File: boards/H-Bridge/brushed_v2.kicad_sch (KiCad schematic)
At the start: 14 parts, among them IC1 TC1108-3.3VDBTR, J1 Prog_Header, J2 CANBus, J3 UART, J4 Encoder, U1 STM32F103C8Tx

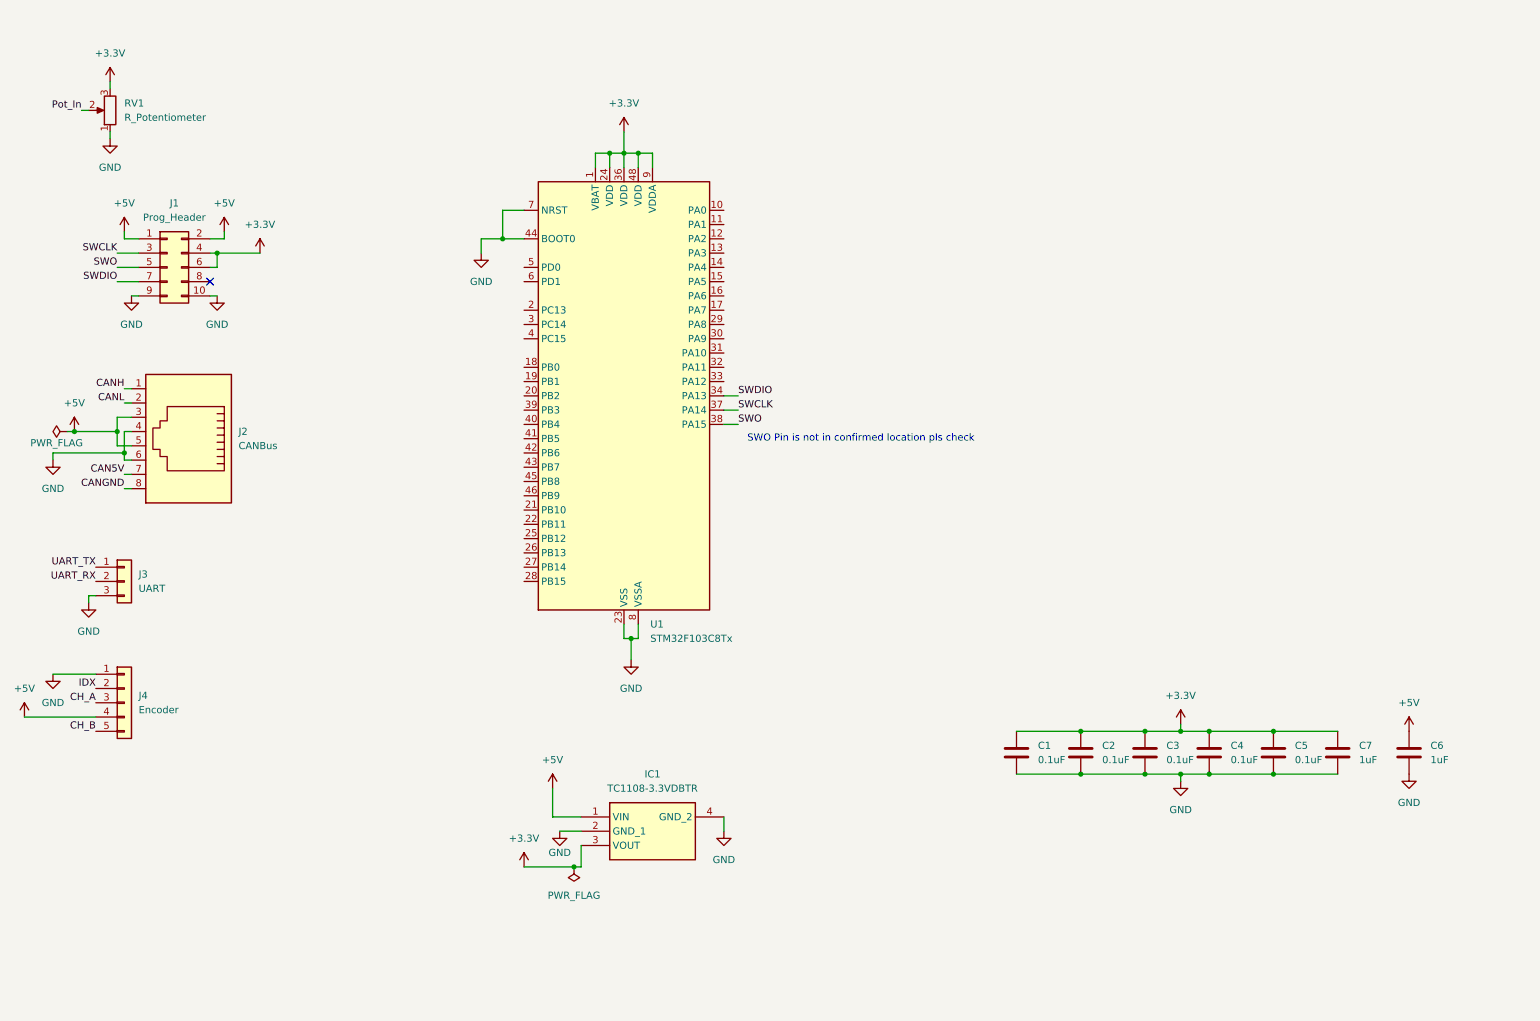
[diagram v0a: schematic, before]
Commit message: Add new sheet for HV, add components
also figured out hierarchical labels
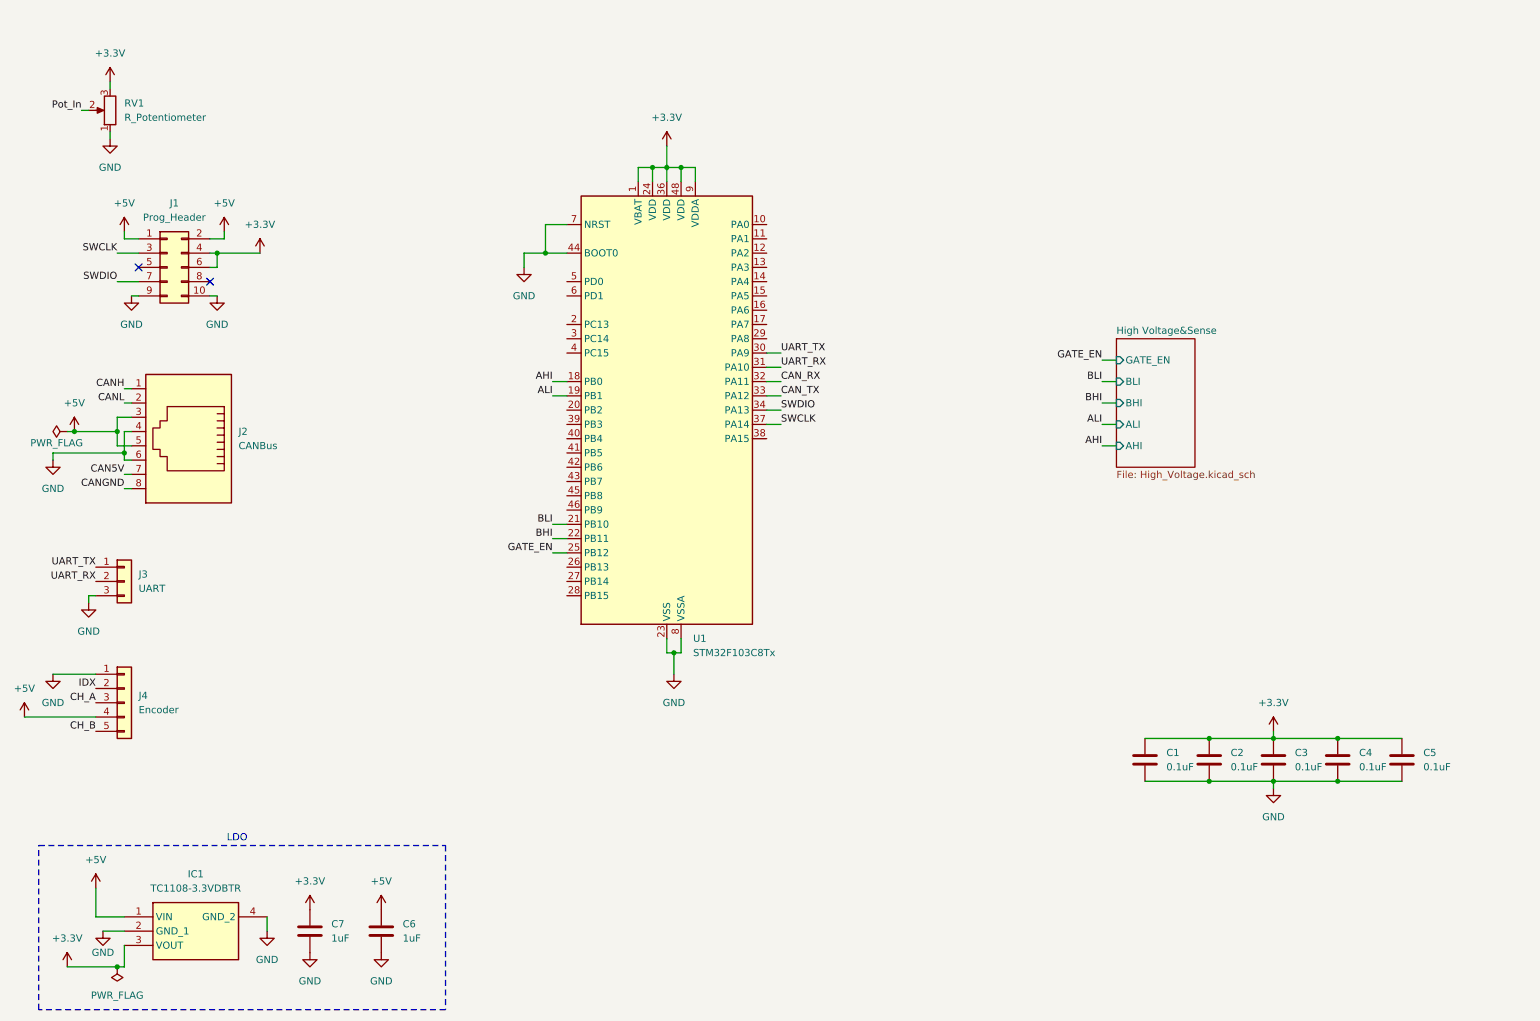
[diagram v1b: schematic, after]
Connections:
- net UART_RX: now also U1.31 (PA10)
- net UART_TX: now also U1.30 (PA9)
- net AHI: now reaches U1.18 (PB0)
- net ALI: now reaches U1.19 (PB1)
- net BLI: now reaches U1.21 (PB10)
- net BHI: now reaches U1.22 (PB11)
- net GATE_EN: now reaches U1.25 (PB12)
- net CAN_RX: now reaches U1.32 (PA11)
- net CAN_TX: now reaches U1.33 (PA12)
- net SWO: no longer names the net of J1.5 (Pin_5)
- net SWO: no longer U1.38 (PA15)
- no-connect marks 1 -> 2
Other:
- added sheet High Voltage&Sense (High_Voltage.kicad_sch)
- note added: "LDO"
- note removed: "SWO Pin is not in confirmed location pls check"
- moved on the sheet: C1, C2, C3, C4, C5, C6, IC1, U1

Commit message: Added symbols + fixed sheet layout, low voltage nearly complete
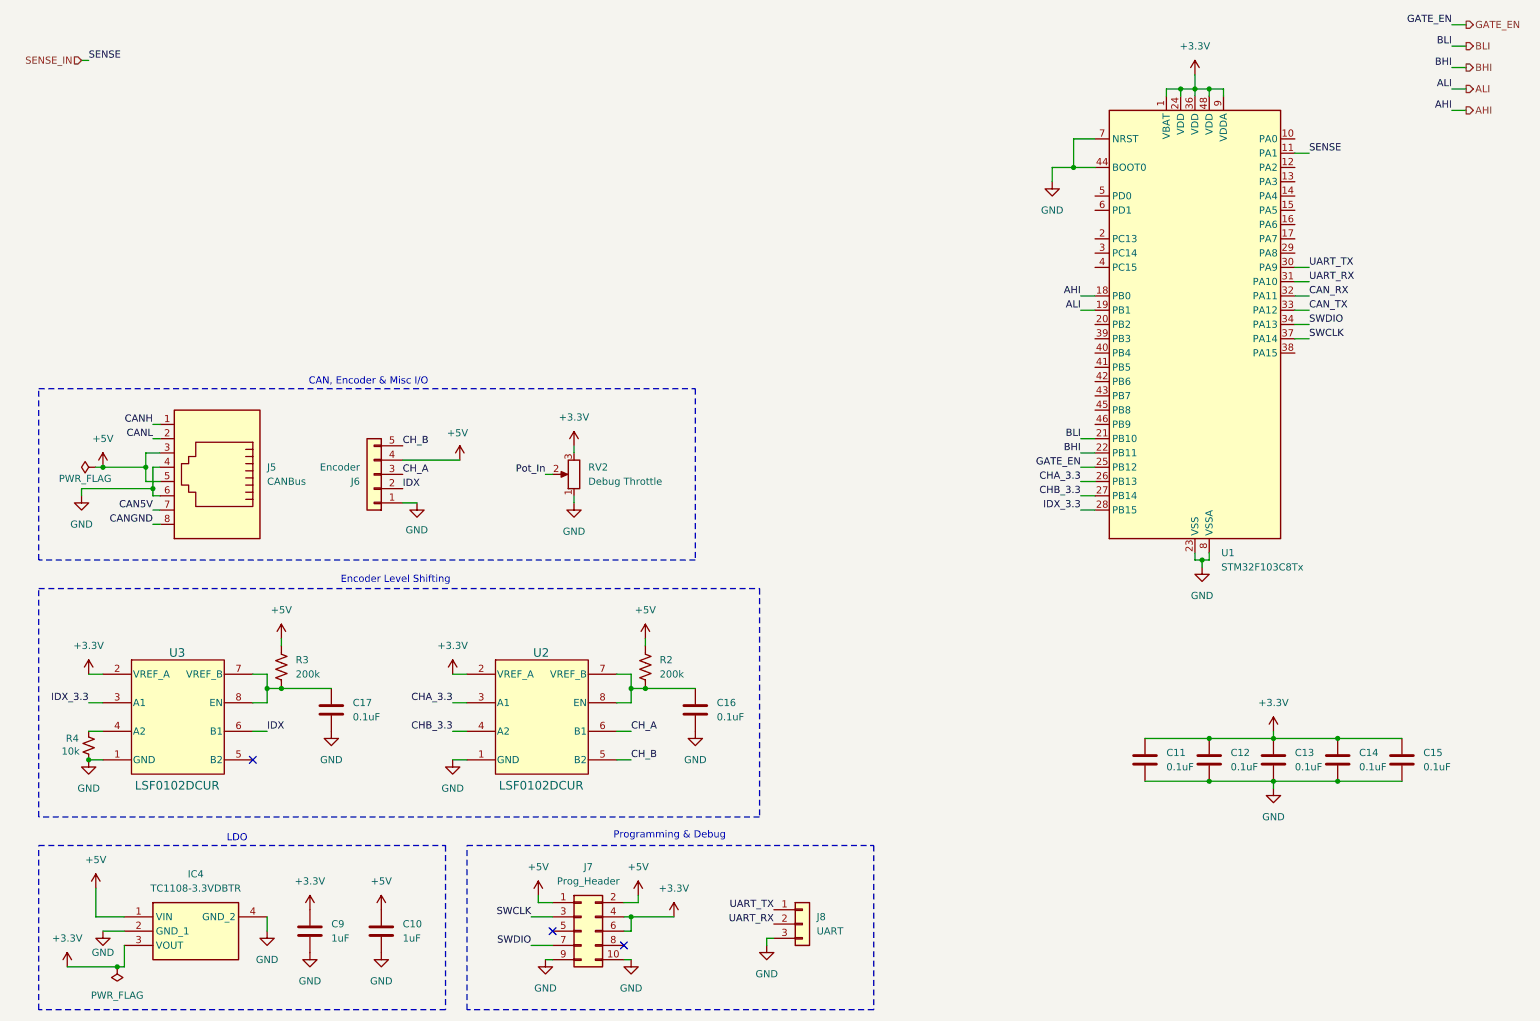
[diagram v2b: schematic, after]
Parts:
- added C16, C17: 0.1uF, symbol Device:C
- added R2, R3: 200k, symbol Device:R_US
- added R4: 10k, symbol Device:R_Small_US
- added U2, U3: LSF0102DCUR, DCU0008A_N, symbol Level_Shifters:LSF0102DCUR
- RV2: renamed from RV1; value R_Potentiometer -> Debug Throttle
- renumbered C6 to C10, C1 to C11, C2 to C12, C3 to C13, C4 to C14, C5 to C15, C7 to C9, IC1 to IC4, J2 to J5, J4 to J6, J1 to J7, J3 to J8
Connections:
- net +3.3V: now also U2.2 (VREF_A), U3.2 (VREF_A)
- net +5V: now also R2.1, R3.1
- net CH_A: now also U2.6 (B1)
- net CH_B: now also U2.5 (B2)
- net GND: now also C16.2, C17.2, R4.1, U2.1 (GND), U3.1 (GND)
- net IDX: now also U3.6 (B1)
- net SENSE_IN: now reaches U1.11 (PA1)
- net CHA_3.3: now reaches U1.26 (PB13)
- net CHA_3.3: now also U2.3 (A1)
- net CHB_3.3: now reaches U1.27 (PB14)
- net CHB_3.3: now also U2.4 (A2)
- net IDX_3.3: now reaches U1.28 (PB15)
- net IDX_3.3: now also U3.3 (A1)
- new net: C17.1, R3.2, U3.7 (VREF_B), U3.8 (EN)
- new net: R4.2, U3.4 (A2)
- new net: C16.1, R2.2, U2.7 (VREF_B), U2.8 (EN)
- no-connect marks 2 -> 3
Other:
- removed sheet High Voltage&Sense
- note added: "CAN, Encoder & Misc I/O"
- note added: "Encoder Level Shifting"
- note added: "Programming & Debug"
- moved on the sheet: J5, J6, J7, J8, RV2, U1

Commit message: finished schematic (i think), added footprints
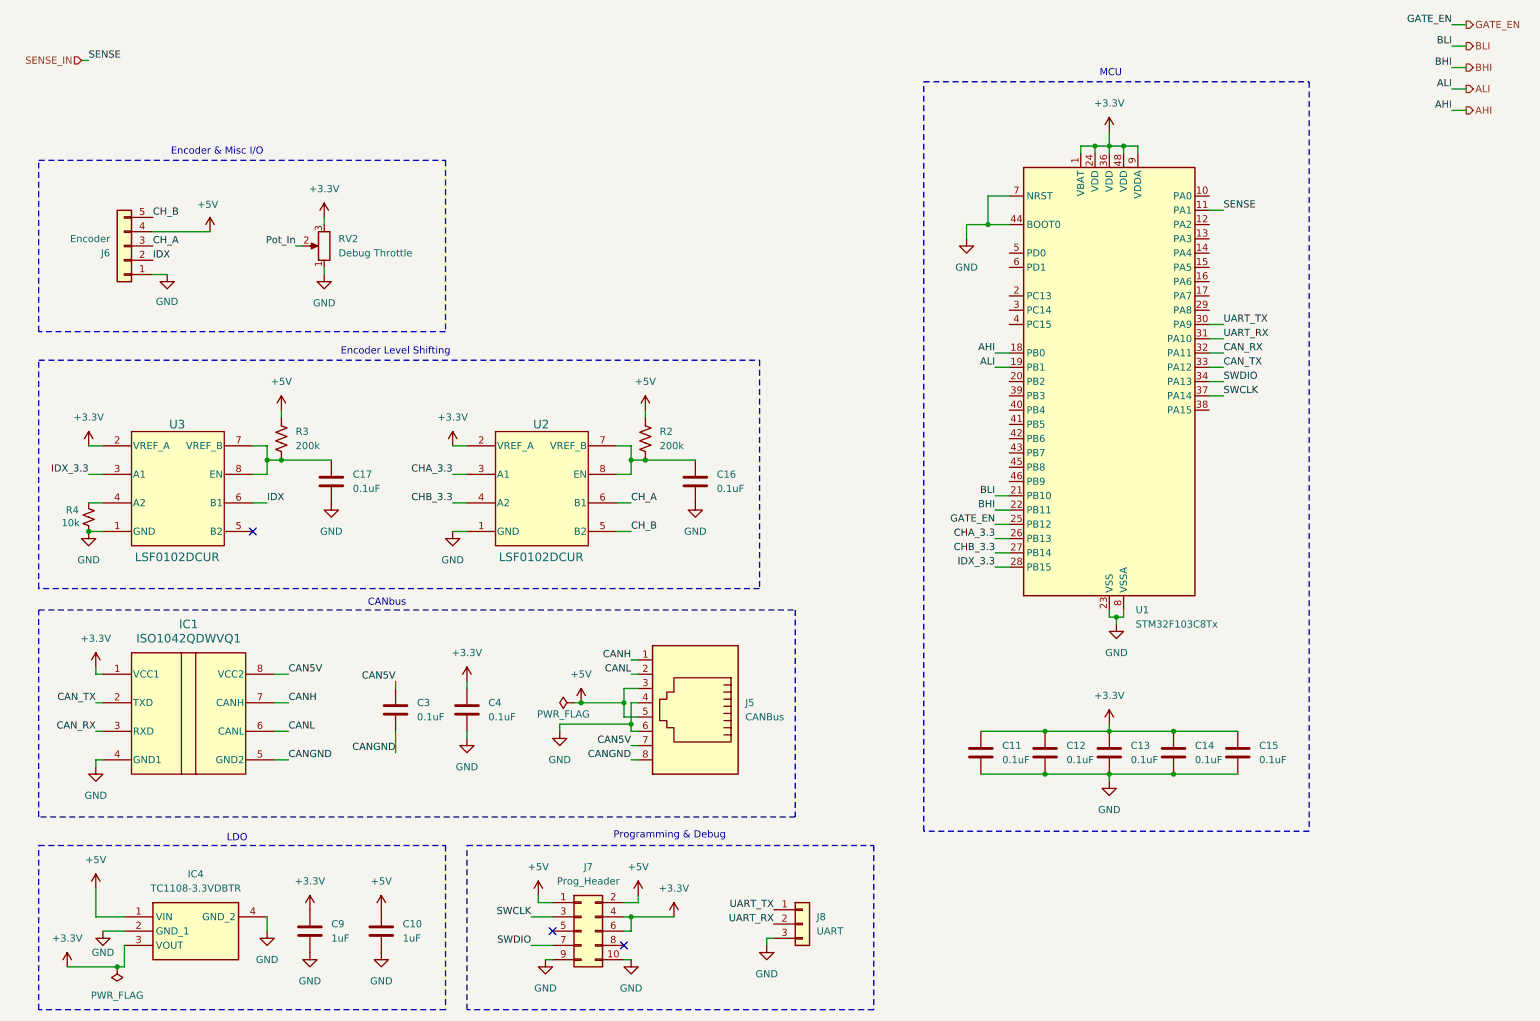
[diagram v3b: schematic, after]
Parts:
- added C3, C4: 0.1uF, symbol Device:C
- added IC1: ISO1042QDWVQ1, CAN Isolators & Trancievers:DWV0008A-IPC_A, symbol CAN Isolators & Trancievers:ISO1042QDWVQ1
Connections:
- net +3.3V: now also C4.1, IC1.1 (VCC1)
- net CAN5V: now also C3.1, IC1.8 (VCC2)
- net CANGND: now also C3.2, IC1.5 (GND2)
- net CANH: now also IC1.7 (CANH)
- net CANL: now also IC1.6 (CANL)
- net CAN_RX: now also IC1.3 (RXD)
- net CAN_TX: now also IC1.2 (TXD)
- net GND: now also C4.2, IC1.4 (GND1)
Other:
- note added: "CANbus"
- note added: "Encoder & Misc I/O"
- note added: "MCU"
- note removed: "CAN, Encoder & Misc I/O"
- moved on the sheet: C11, C12, C13, C14, C15, C16, C17, J5, J6, R2, R3, R4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

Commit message: finished schematic, added footprint assignments
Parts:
- added C18: 4.7uF, Capacitor_SMD:C_0402_1005Metric, symbol Device:C
- C10, C11, C12, C13, C14, C15, C16, C17, C3, C4, C9: footprint (none) -> Capacitor_SMD:C_0402_1005Metric
- IC4: footprint SOT230P700X180-4N -> Package_TO_SOT_SMD:SOT-223
- J5: footprint (none) -> Connector_RJ:RJ45_Amphenol_54602-x08_Horizontal
- J6: footprint (none) -> Connector_PinHeader_2.54mm:PinHeader_1x05_P2.54mm_Vertical
- J7: footprint (none) -> Connector_PinHeader_2.54mm:PinHeader_2x05_P2.54mm_Vertical
- J8: footprint (none) -> Connector_PinHeader_2.54mm:PinHeader_1x03_P2.54mm_Vertical
- R2, R3, R4: footprint (none) -> Resistor_SMD:R_0402_1005Metric
- RV2: footprint Potentiometer_THT:P120PKY25BR10K -> Potentiometers THD:P120PKY25BR10K
- U2, U3: footprint DCU0008A_N -> Package_SO:SSOP-8_2.95x2.8mm_P0.65mm
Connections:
- net +3.3V: now also C18.1
- net GND: now also C18.2
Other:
- moved on the sheet: C11, C12, C13, C14, C15, U1

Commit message: started pcb layout, added small LEDs and SWO to schematic
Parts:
- added D1, D2: LED, Capacitor_SMD:C_0603_1608Metric, symbol Device:LED
- added R10, R11: 1k, Resistor_SMD:R_0402_1005Metric, symbol Device:R_US
- added R9: 10k, Resistor_SMD:R_0402_1005Metric, symbol Device:R_US
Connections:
- net +3.3V: now also U1.7 (NRST)
- net GND: now also D1.1 (K), D2.1 (K), R9.2; no longer U1.44 (BOOT0), U1.7 (NRST)
- net SENSE_IN: now also U1.17 (PA7); no longer U1.11 (PA1)
- net SWO: now reaches J7.5 (Pin_5)
- net SWO: now also U1.39 (PB3)
- net LED_2: now reaches U1.40 (PB4)
- net LED_2: now also R11.1
- net LED_1: now reaches U1.41 (PB5)
- net LED_1: now also R10.1
- net Pot_In renamed POT_IN
- net POT_IN: now also U1.11 (PA1)
- new net: D2.2 (A), R11.2
- new net: R9.1, U1.44 (BOOT0)
- new net: D1.2 (A), R10.2
- no-connect marks 3 -> 20
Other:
- note added: "LED Debug"
- note added: "Programming & Ext Communication"
- note removed: "Programming & Debug"

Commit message: modified pwm signals to be on same timer
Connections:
- net AHI: now also U1.16 (PA6); no longer U1.18 (PB0)
- net ALI: now also U1.17 (PA7); no longer U1.19 (PB1)
- net BHI: now also U1.19 (PB1); no longer U1.22 (PB11)
- net BLI: now also U1.18 (PB0); no longer U1.21 (PB10)
- net SENSE_IN: now also U1.13 (PA3); no longer U1.17 (PA7)
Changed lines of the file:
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@@
 	)
 	(no_connect
-		(at 229.87 62.23)
+		(at 194.31 100.33)
 	)
 	(no_connect
@@
 	)
 	(no_connect
-		(at 229.87 54.61)
-	)
-	(no_connect
 		(at 194.31 57.15)
 	)
@@
 	)
 	(no_connect
+		(at 194.31 102.87)
+	)
+	(no_connect
 		(at 194.31 90.17)
 	)
@@
 	(wire
 		(pts
-			(xy 229.87 64.77) (xy 232.41 64.77)
-		)
-		(stroke
-			(width 0)
-			(type default)
-		)
-	)
-	(wire
-		(pts
 			(xy 58.42 96.52) (xy 60.96 96.52)
 		)
@@
 	(wire
 		(pts
-			(xy 191.77 102.87) (xy 194.31 102.87)
-		)
-		(stroke
-			(width 0)
-			(type default)
-		)
-	)
-	(wire
-		(pts
 			(xy 29.21 101.6) (xy 31.75 101.6)
 		)
@@
 	(wire
 		(pts
-			(xy 191.77 100.33) (xy 194.31 100.33)
-		)
-		(stroke
-			(width 0)
-			(type default)
-		)
-	)
-	(wire
-		(pts
 			(xy 213.36 121.92) (xy 213.36 123.19)
 		)
@@
 		(pts
 			(xy 113.03 140.97) (xy 125.73 140.97)
+		)
+		(stroke
+			(width 0)
+			(type default)
+		)
+	)
+	(wire
+		(pts
+			(xy 232.41 54.61) (xy 229.87 54.61)
 		)
 		(stroke
@@
 		)
 	)
+	(label "BLI"
+		(at 191.77 74.93 180)
+		(effects
+			(font
+				(size 1.27 1.27)
+			)
+			(justify right bottom)
+		)
+	)
 	(label "CHB_3.3"
 		(at 93.98 101.6 180)
@@
 		)
 	)
-	(label "ALI"
-		(at 191.77 77.47 180)
-		(effects
-			(font
-				(size 1.27 1.27)
-			)
-			(justify right bottom)
-		)
-	)
 	(label "UART_RX"
 		(at 232.41 72.39 0)
@@
 		)
 	)
+	(label "AHI"
+		(at 229.87 62.23 0)
+		(effects
+			(font
+				(size 1.27 1.27)
+			)
+			(justify left bottom)
+		)
+	)
 	(label "LED_2"
 		(at 109.22 44.45 180)
@@
 	)
 	(label "SENSE"
-		(at 232.41 64.77 0)
+		(at 232.41 54.61 0)
+		(effects
+			(font
+				(size 1.27 1.27)
+			)
+			(justify left bottom)
+		)
+	)
+	(label "ALI"
+		(at 229.87 64.77 0)
 		(effects
 			(font
@@
 		)
 	)
-	(label "AHI"
-		(at 191.77 74.93 180)
-		(effects
-			(font
-				(size 1.27 1.27)
-			)
-			(justify right bottom)
-		)
-	)
 	(label "SENSE"
 		(at 29.21 22.86 0)
@@
 		)
 	)
-	(label "BLI"
-		(at 191.77 100.33 180)
-		(effects
-			(font
-				(size 1.27 1.27)
-			)
-			(justify right bottom)
-		)
-	)
 	(label "CHA_3.3"
 		(at 93.98 96.52 180)
@@
 		)
 	)
-	(label "BHI"
-		(at 191.77 102.87 180)
-		(effects
-			(font
-				(size 1.27 1.27)
-			)
-			(justify right bottom)
-		)
-	)
 	(label "CHA_3.3"
 		(at 191.77 107.95 180)
@@
 		(effects
 			(font
+				(size 1.27 1.27)
+			)
+			(justify right bottom)
+		)
+	)
+	(label "BHI"
+		(at 191.77 77.47 180)
+		(effects
+			(font

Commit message: changed pins for encoder to match embedded
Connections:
- net CHA_3.3: now also U1.42 (PB6); no longer U1.26 (PB13)
- net CHB_3.3: now also U1.43 (PB7); no longer U1.27 (PB14)
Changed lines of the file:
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@@
+	)
+	(no_connect
+		(at 194.31 107.95)
+	)
+	(no_connect
+		(at 194.31 110.49)
 	)
 	(no_connect
@@
 	)
 	(no_connect
-		(at 194.31 92.71)
-	)
-	(no_connect
 		(at 229.87 57.15)
 	)
@@
 	)
 	(no_connect
-		(at 194.31 90.17)
-	)
-	(no_connect
 		(at 124.46 180.34)
 	)
@@
 	(wire
 		(pts
+			(xy 232.41 62.23) (xy 229.87 62.23)
+		)
+		(stroke
+			(width 0)
+			(type default)
+		)
+	)
+	(wire
+		(pts
 			(xy 83.82 142.24) (xy 83.82 146.05)
 		)
@@
 	(wire
 		(pts
+			(xy 191.77 92.71) (xy 194.31 92.71)
+		)
+		(stroke
+			(width 0)
+			(type default)
+		)
+	)
+	(wire
+		(pts
 			(xy 195.58 149.86) (xy 207.01 149.86)
 		)
@@
 	(wire
 		(pts
-			(xy 194.31 110.49) (xy 191.77 110.49)
-		)
-		(stroke
-			(width 0)
-			(type default)
-		)
-	)
-	(wire
-		(pts
 			(xy 191.77 85.09) (xy 194.31 85.09)
 		)
@@
 	(wire
 		(pts
+			(xy 191.77 90.17) (xy 194.31 90.17)
+		)
+		(stroke
+			(width 0)
+			(type default)
+		)
+	)
+	(wire
+		(pts
 			(xy 194.31 46.99) (xy 191.77 46.99)
 		)
@@
 	(wire
 		(pts
+			(xy 232.41 64.77) (xy 229.87 64.77)
+		)
+		(stroke
+			(width 0)
+			(type default)
+		)
+	)
+	(wire
+		(pts
 			(xy 29.21 22.86) (xy 27.94 22.86)
 		)
@@
 		(pts
 			(xy 66.04 55.88) (xy 67.31 55.88)
-		)
-		(stroke
-			(width 0)
-			(type default)
-		)
-	)
-	(wire
-		(pts
-			(xy 191.77 107.95) (xy 194.31 107.95)
 		)
 		(stroke
@@
 	)
 	(label "AHI"
-		(at 229.87 62.23 0)
+		(at 232.41 62.23 0)
 		(effects
 			(font
@@
 	)
 	(label "CHB_3.3"
-		(at 191.77 110.49 180)
+		(at 191.77 92.71 180)
 		(effects
 			(font
@@
 	)
 	(label "ALI"
-		(at 229.87 64.77 0)
+		(at 232.41 64.77 0)
 		(effects
 			(font
@@
 	)
 	(label "CHA_3.3"
-		(at 191.77 107.95 180)
-		(effects
-			(font
+		(at 191.77 90.17 180)
+		(effects
+			(font

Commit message: finished layout, need to add silk key
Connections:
- net CHA_3.3: now also U2.4 (A2); no longer U2.3 (A1)
- net CHB_3.3: now also U2.3 (A1); no longer U2.4 (A2)
- net CH_A: now also U2.5 (B2); no longer U2.6 (B1)
- net CH_B: now also U2.6 (B1); no longer U2.5 (B2)
- net IDX_3.3: now also U1.45 (PB8); no longer U1.28 (PB15)
